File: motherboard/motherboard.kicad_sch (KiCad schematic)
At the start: 38 parts, among them J20 CM3588 Hirose Connector, J22 BATTERY IN, U17 TPS564257DRLR, U20 TPS564257DRLR, U23 TPS564257DRLR, U24 RT9193-18GB

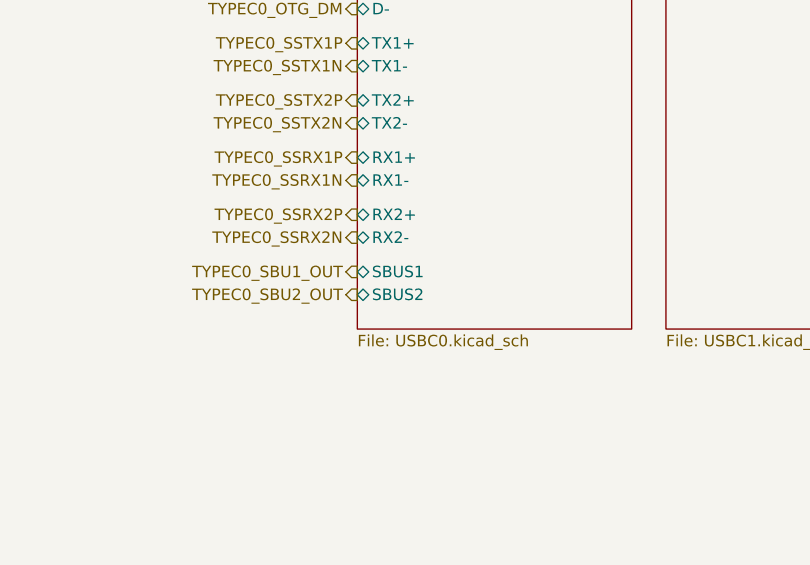
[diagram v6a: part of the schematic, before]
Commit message: v0.2 < 50 unrouted
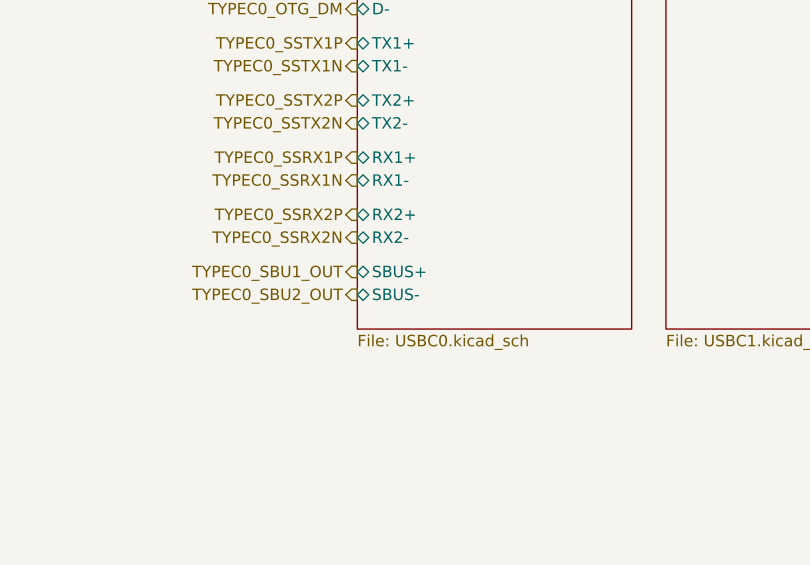
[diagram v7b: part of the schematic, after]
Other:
- sheet USBC0 ports: added SBUS+, SBUS-; removed SBUS1, SBUS2
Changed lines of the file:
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@@
-			)
-		)
-		(pin "SBUS2" bidirectional
-			(at 139.7 314.96 180)
-			(effects
-				(font
-					(size 1.27 1.27)
-				)
-				(justify left)
 			)
 		)
@@
 			)
 		)
-		(pin "SBUS1" bidirectional
+		(pin "TX2-" bidirectional
+			(at 139.7 295.91 180)
+			(effects
+				(font
+					(size 1.27 1.27)
+				)
+				(justify left)
+			)
+		)
+		(pin "SBUS+" bidirectional
 			(at 139.7 312.42 180)
 			(effects
@@
 			)
 		)
-		(pin "TX2-" bidirectional
-			(at 139.7 295.91 180)
+		(pin "SBUS-" bidirectional
+			(at 139.7 314.96 180)
 			(effects
 				(font

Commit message: v0.2 almost ready for tapeout
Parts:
- added C80, C81, C82: 10uF, Capacitor_SMD:C_0603_1608Metric, symbol Device:C_Small
- added H1, H2, H3, H4: M2, MountingHole:MountingHole_2.2mm_M2_Pad_Via, symbol Mechanical:MountingHole
- added J21: VDD EXT 2, Connector_PinHeader_2.54mm:PinHeader_1x02_P2.54mm_Vertical, symbol Connector_Generic:Conn_01x02
- added J9: VDD EXT, Connector_PinHeader_2.54mm:PinHeader_1x02_P2.54mm_Vertical, symbol Connector_Generic:Conn_01x02
- C39, C44, C49: value 22uF -> 10uF
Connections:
- net GND: now also C80.2, C81.2, C82.2, J21.1 (Pin_1), J9.1 (Pin_1)
- net VDD: now also C80.1, C81.1, C82.1, J21.2 (Pin_2), J9.2 (Pin_2)
